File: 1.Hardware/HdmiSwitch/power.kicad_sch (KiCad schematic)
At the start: 12 parts

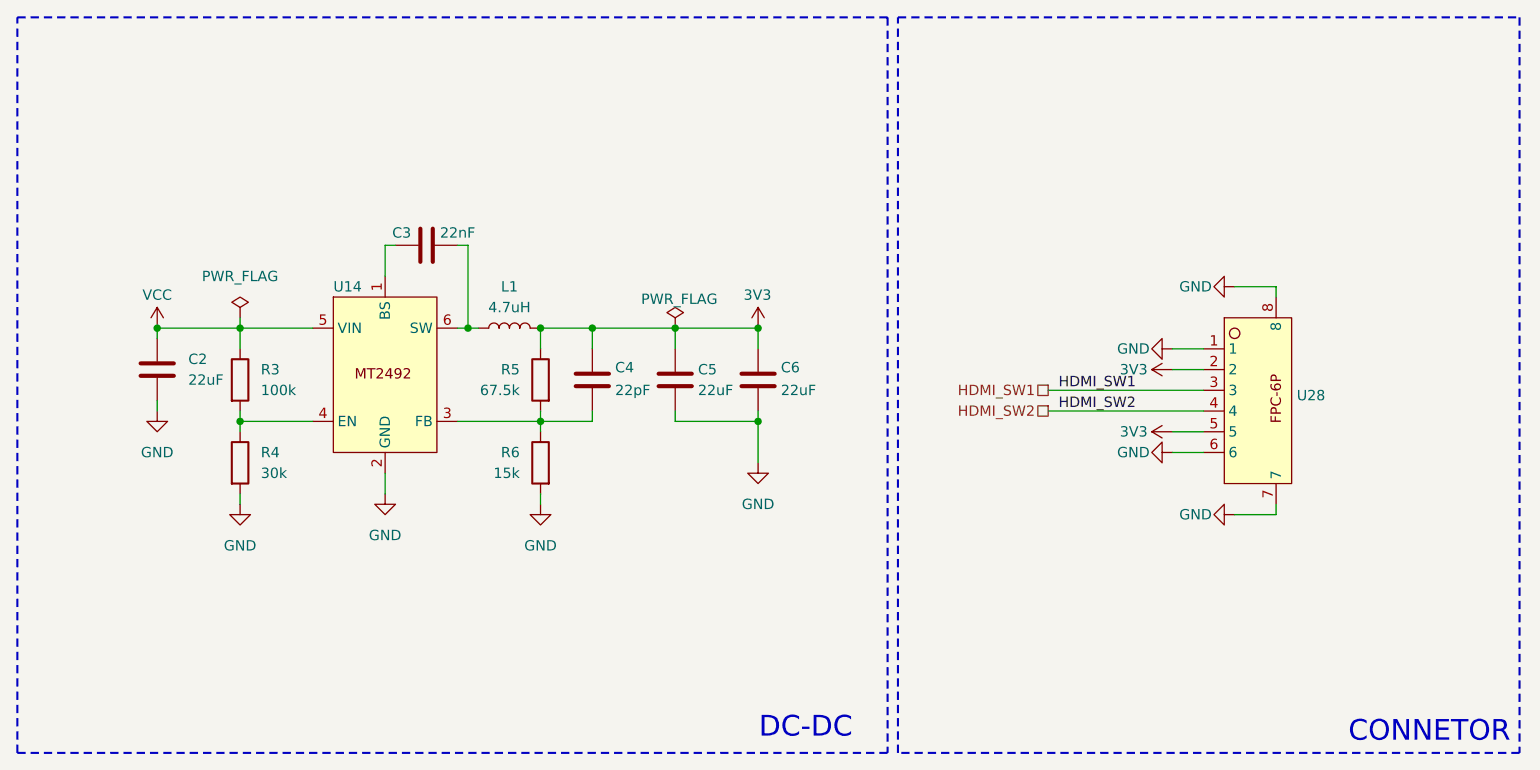
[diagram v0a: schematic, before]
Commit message: 为HDMISwitch模块添加了封装模型
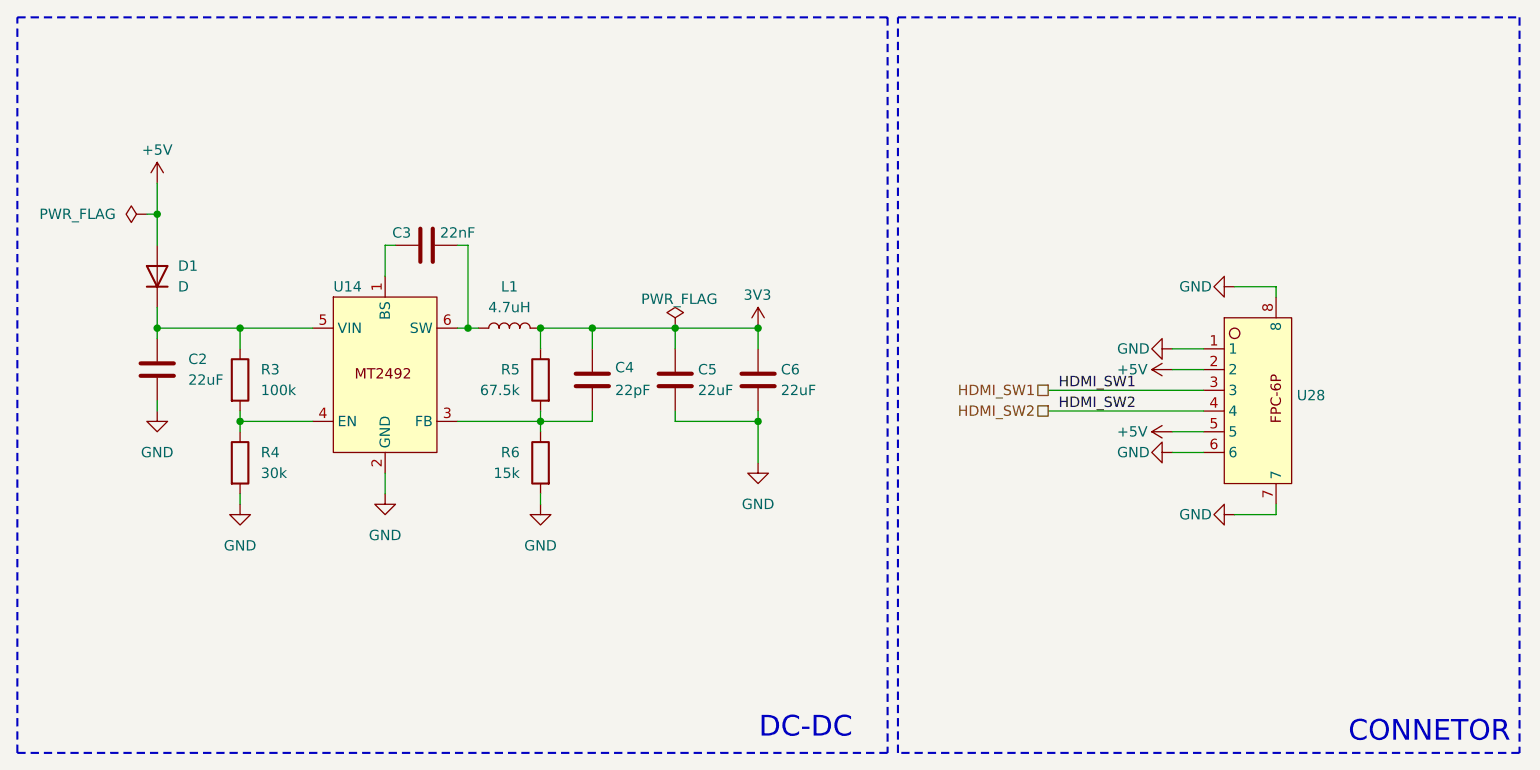
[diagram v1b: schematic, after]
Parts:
- added D1: D, HdmiSwitch:二极管, symbol Device:D
- C2, C5, C6: footprint (none) -> Capacitor_SMD:C_0805_2012Metric
- C3, C4: footprint (none) -> Capacitor_SMD:C_0402_1005Metric
- L1: footprint (none) -> HdmiSwitch:CD32
- R3, R4, R5, R6: footprint (none) -> Resistor_SMD:R_0402_1005Metric
- U14: footprint (none) -> Package_TO_SOT_SMD:SOT-23-6
- U28: footprint (none) -> HdmiSwitch:FPC座子6P翻盖下接
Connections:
- net 3V3: no longer U28.2, U28.5
- net VCC: no longer names the net of C2.1, R3.1, U14.5 (VIN)
- net VCC: now also D1.1 (K)
- new net +5V: D1.2 (A), U28.2, U28.5
